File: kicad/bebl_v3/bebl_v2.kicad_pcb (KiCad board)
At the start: 2 copper layers, 80 x 44 mm, 66 parts, among them P1 ISP, P10 LED_DRL, P12 CHG_LED, P13 LED_CHG, P2 FTDI, P3 Ext_LiPo, P4 USB-Micro, P5 DRV_1, P6 LED_1, P7 DRV_2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

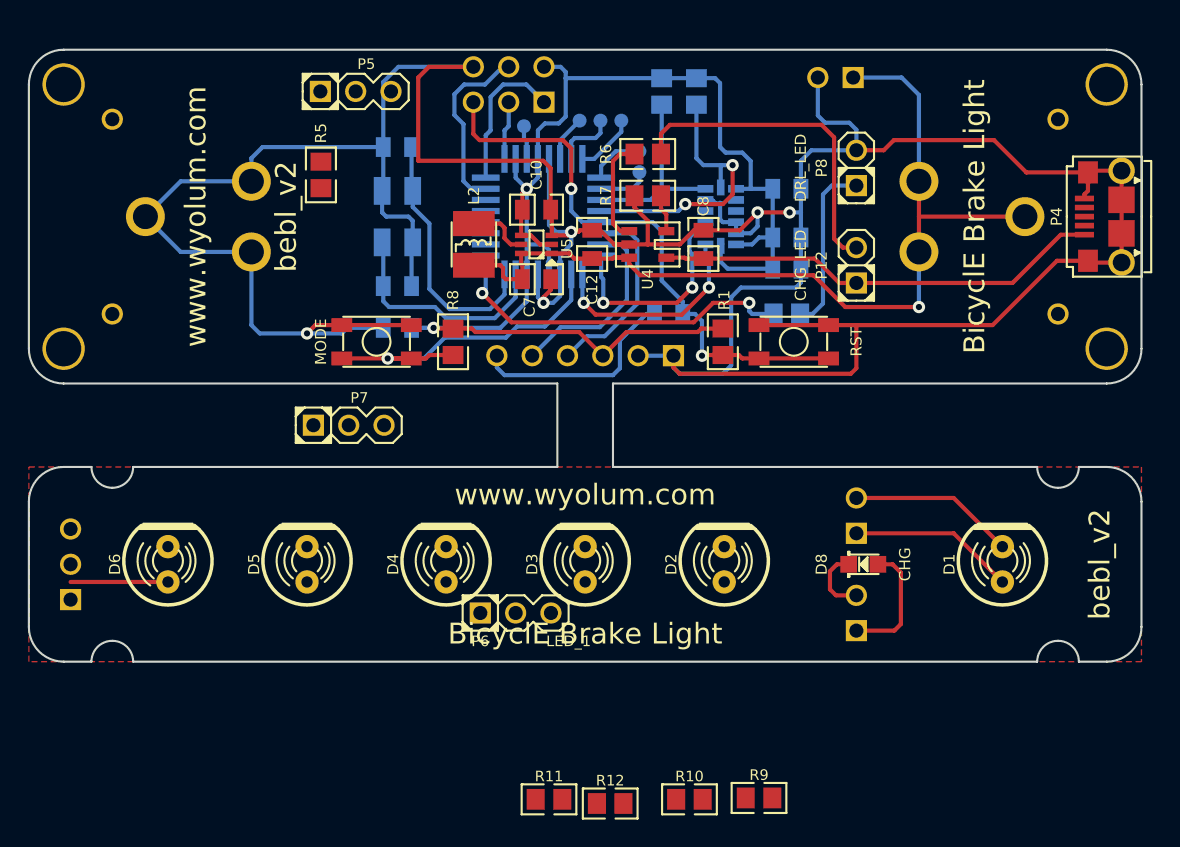
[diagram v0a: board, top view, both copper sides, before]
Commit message: revised layout for driverless version, in folder bebl_v3. Work in progress
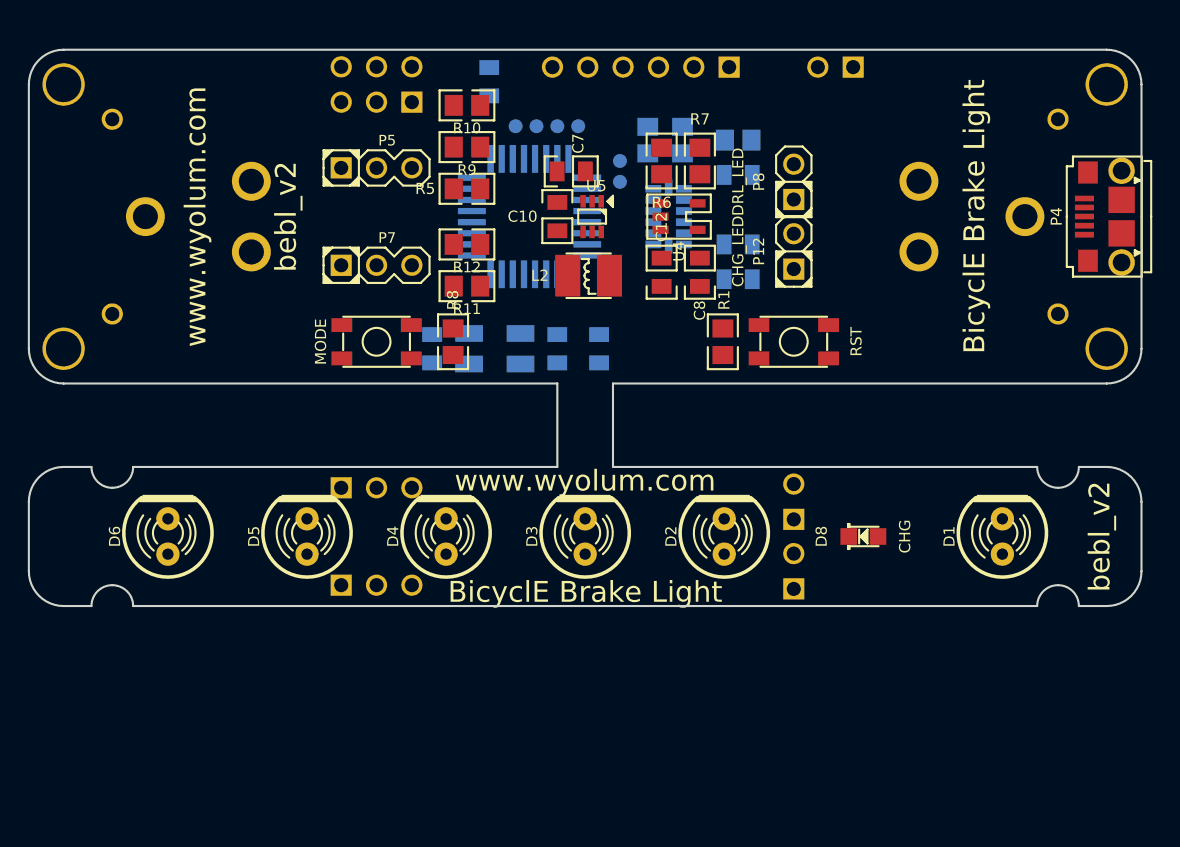
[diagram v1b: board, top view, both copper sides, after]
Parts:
- P6: moved to B.Cu
- moved R10 52.4 mm to (65.5, 42.0), turned to 180 degrees
- moved R9 51.3 mm to (65.5, 45.0), turned to 180 degrees
- moved R12 41.5 mm to (65.5, 52.0), turned to 180 degrees
- moved R11 37.4 mm to (65.5, 55.0), turned to 180 degrees
- moved P9 22.1 mm to (59.0, 76.5), turned to 0 degrees
- moved P2 21.1 mm to (78.0, 39.2)
- moved C4 21.1 mm to (67.1, 40.3), turned to 90 degrees
- moved C2 14.7 mm to (63.0, 59.5), turned to 270 degrees
- moved C3 14.6 mm to (75.0, 59.5), turned to 90 degrees
- moved P6 13.5 mm to (59.0, 69.5)
- moved R4 13.0 mm to (85.0, 44.5)
- moved C1 12.3 mm to (72.0, 59.5), turned to 270 degrees
- moved X1 11.8 mm to (67.5, 59.5), turned to 180 degrees
- moved P7 11.7 mm to (59.0, 53.5)
- moved R5 10.5 mm to (65.5, 48.0), turned to 180 degrees
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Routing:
- net GND: track 263.1 -> 0.00 mm, vias 5 -> 0
- net +3.3V: track 102.0 -> 0.00 mm, vias 2 -> 0
- net /BAT: track 67.4 -> 0.00 mm, vias 1 -> 0
- net /RESET: track 41.3 -> 0.00 mm, vias 2 -> 0
- net /VUSB: track 32.3 -> 0.00 mm
- net /MODE: track 26.6 -> 0.00 mm, vias 1 -> 0
- net /LED_D1: track 25.9 -> 0.00 mm, vias 2 -> 0
- net Net-(P12-Pad2): track 23.7 -> 0.00 mm
- net /SCL: track 20.3 -> 0.00 mm, vias 2 -> 0
- net /PB7: track 18.6 -> 0.00 mm
- net /PB6: track 16.6 -> 0.00 mm
- net /ACL_INT1: track 15.5 -> 0.00 mm, vias 2 -> 0
- net Net-(C4-Pad1): track 15.4 -> 0.00 mm
- net /ACL_INT2: track 15.3 -> 0.00 mm, vias 2 -> 0
- net /TXD: track 14.1 -> 0.00 mm
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- removed copper zone on F.Cu, net /D1K
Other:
- board size 80 x 44 mm -> 80 x 40 mm

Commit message: revised layout for driverless version, in folder bebl_v3. Check PDF files in GERBER folder
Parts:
- moved R1 3.24 mm to (80.8, 58.2), turned to 180 degrees
- moved C7 2.26 mm to (75.2, 46.5)
- moved R8 1.25 mm to (65.5, 58.2), turned to 0 degrees
- moved B1 0.50 mm to (72.5, 43.5)
- moved B2 0.50 mm to (74.0, 43.5)
- moved B5 0.50 mm to (69.5, 43.5)
- moved B6 0.50 mm to (71.0, 43.5)
- moved L2 0.50 mm to (74.8, 54.2)
- turned D1 to 180 degrees
- turned D2 to 180 degrees
- turned D3 to 180 degrees
- turned D4 to 180 degrees
- turned D5 to 180 degrees
- turned D6 to 180 degrees
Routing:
- net GND: track 0.00 -> 261.3 mm, vias 0 -> 2
- net +3.3V: track 0.00 -> 129.1 mm
- net /LED_GND: track 0.00 -> 95.8 mm
- net /RESET: track 0.00 -> 87.5 mm, vias 0 -> 2
- net /BAT: track 0.00 -> 66.1 mm
- net /LED_D1: track 0.00 -> 48.1 mm, vias 0 -> 2
- net /VUSB: track 0.00 -> 33.0 mm
- net /MODE: track 0.00 -> 25.5 mm, vias 0 -> 1
- net Net-(D2-Pad1): track 0.00 -> 25.2 mm
- net Net-(P12-Pad2): track 0.00 -> 22.2 mm, vias 0 -> 1
- net /D1A: track 0.00 -> 21.2 mm
- net /SCL: track 0.00 -> 20.4 mm, vias 0 -> 2
- net /TXD: track 0.00 -> 18.0 mm, vias 0 -> 1
- net Net-(D3-Pad1): track 0.00 -> 17.7 mm
- net /RXD: track 0.00 -> 16.8 mm, vias 0 -> 2
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- added copper zone on F.Cu, net /LED_GND
- added copper zone on B.Cu, net GND
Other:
- board text added: "+x"
- board text added: "+y"
- board text added: "-z"

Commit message: corrected accel x/y/z markings on silk legend
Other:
- board text added: "+z"
- board text removed: "-z"
